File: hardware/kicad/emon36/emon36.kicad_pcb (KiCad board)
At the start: 4 copper layers, 80.6 x 104.1 mm, 236 parts, among them J1 MJ-3523-SMT, J10 MJ-3523-SMT, J11 MJ-3523-SMT, J12 MJ-3523-SMT, J13 MJ-3523-SMT, J14 MJ-3523-SMT, J15 MJ-3523-SMT, J16 MJ-3523-SMT, J17 MJ-3523-SMT, J18 MJ-3523-SMT, J19 MJ-3523-SMT, J2 MJ-3523-SMT, J20 MJ-3523-SMT, J21 MJ-3523-SMT, J22 MJ-3523-SMT, J23 MJ-3523-SMT, J24 MJ-3523-SMT, J25 MJ-3523-SMT, J26 MJ-3523-SMT, J27 MJ-3523-SMT, J28 MJ-3523-SMT, J29 MJ-3523-SMT, J3 MJ-3523-SMT, J30 MJ-3523-SMT, J31 MJ-3523-SMT, J32 MJ-3523-SMT, J33 MJ-3523-SMT, J34 MJ-3523-SMT, J35 MJ-3523-SMT, J36 MJ-3523-SMT, J4 MJ-3523-SMT, J5 MJ-3523-SMT, J6 MJ-3523-SMT, J7 MJ-3523-SMT, J8 MJ-3523-SMT, J9 MJ-3523-SMT, U1 ESP32-C3-WROOM-02-N4

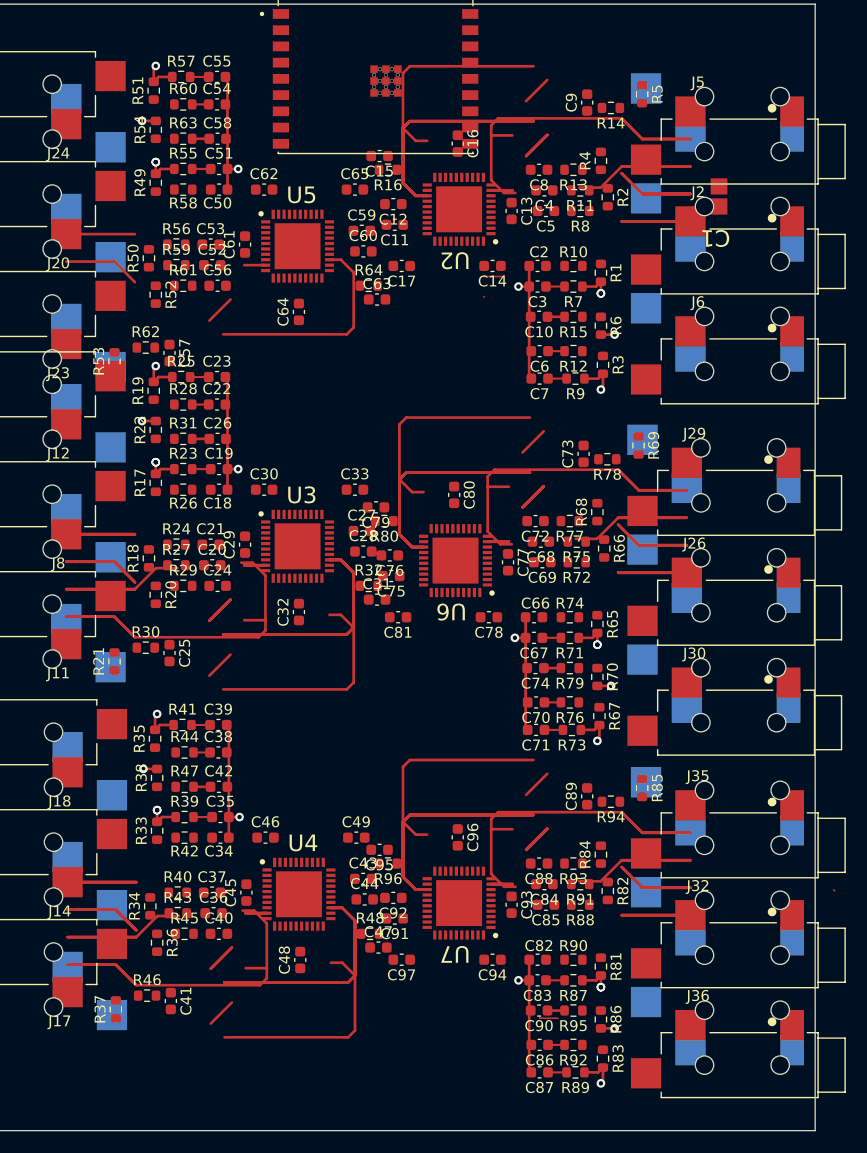
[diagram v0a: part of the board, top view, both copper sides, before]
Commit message: Add preliminary USB interface
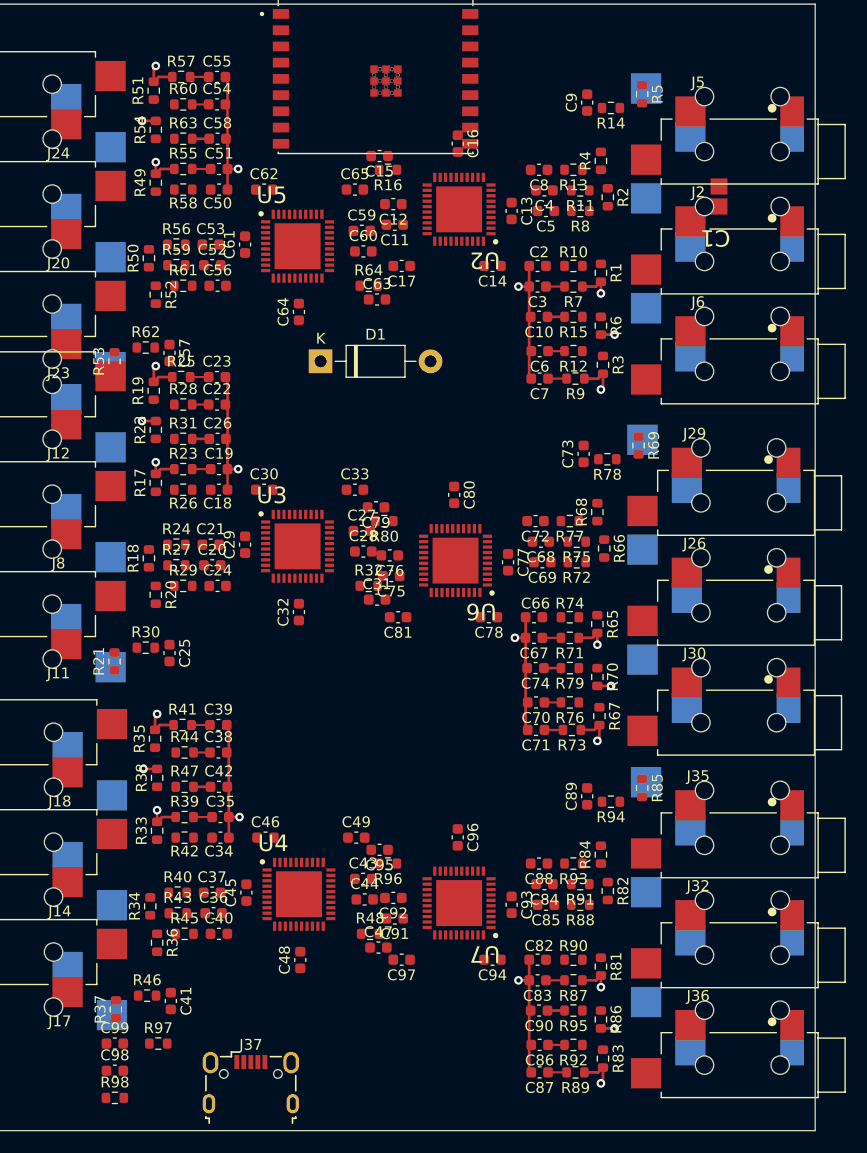
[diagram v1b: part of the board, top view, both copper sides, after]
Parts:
- added C98: 22pF, Capacitor_SMD:C_0603_1608Metric, F.Cu at (40.6, 140.1)
- added C99: 22pF, Capacitor_SMD:C_0603_1608Metric, F.Cu at (40.6, 137.6)
- added D1: 1N5819, Diode_THT:D_DO-41_SOD81_P10.16mm_Horizontal, F.Cu at (59.6, 74.5)
- added J37: USB_B_Micro, Connector_USB:USB_Micro-B_Wuerth_629105150521, F.Cu at (53.2, 141.2)
- added R97: 0, Resistor_SMD:R_0603_1608Metric, F.Cu at (44.6, 137.6)
- added R98: 0, Resistor_SMD:R_0603_1608Metric, F.Cu at (40.6, 142.6)
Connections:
- U1 pad 13: unconnected-(U1-Pad13) -> Net-(U1-Pad13)
- U1 pad 14: unconnected-(U1-Pad14) -> Net-(U1-Pad14)
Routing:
- net GND: track 304.4 -> 115.0 mm, vias 30 -> 24
- net /CH3/ID_P: track 113.0 -> 0.00 mm
- net /CH5/ID_P: track 113.0 -> 0.00 mm
- net /CH2/ID_P: track 110.2 -> 0.00 mm
- net /CH0/ID_P: track 110.2 -> 0.00 mm
- net /CH1/ID_P: track 92.8 -> 0.00 mm
- net Net-(J32-Pad2): track 36.5 -> 0.00 mm
- net Net-(J2-Pad2): track 36.5 -> 0.00 mm
- net Net-(J8-Pad2): track 36.5 -> 0.00 mm
- net Net-(J14-Pad2): track 36.5 -> 0.00 mm
- net Net-(J26-Pad2): track 36.5 -> 0.00 mm
- net /CH4/ID_P: track 30.0 -> 0.00 mm
- net unconnected-(U1-Pad15): track 20.1 -> 0.00 mm
- net Net-(J20-Pad2): track 6.35 -> 0.00 mm
- net /CH3/IB_P: track 5.94 -> 0.00 mm
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
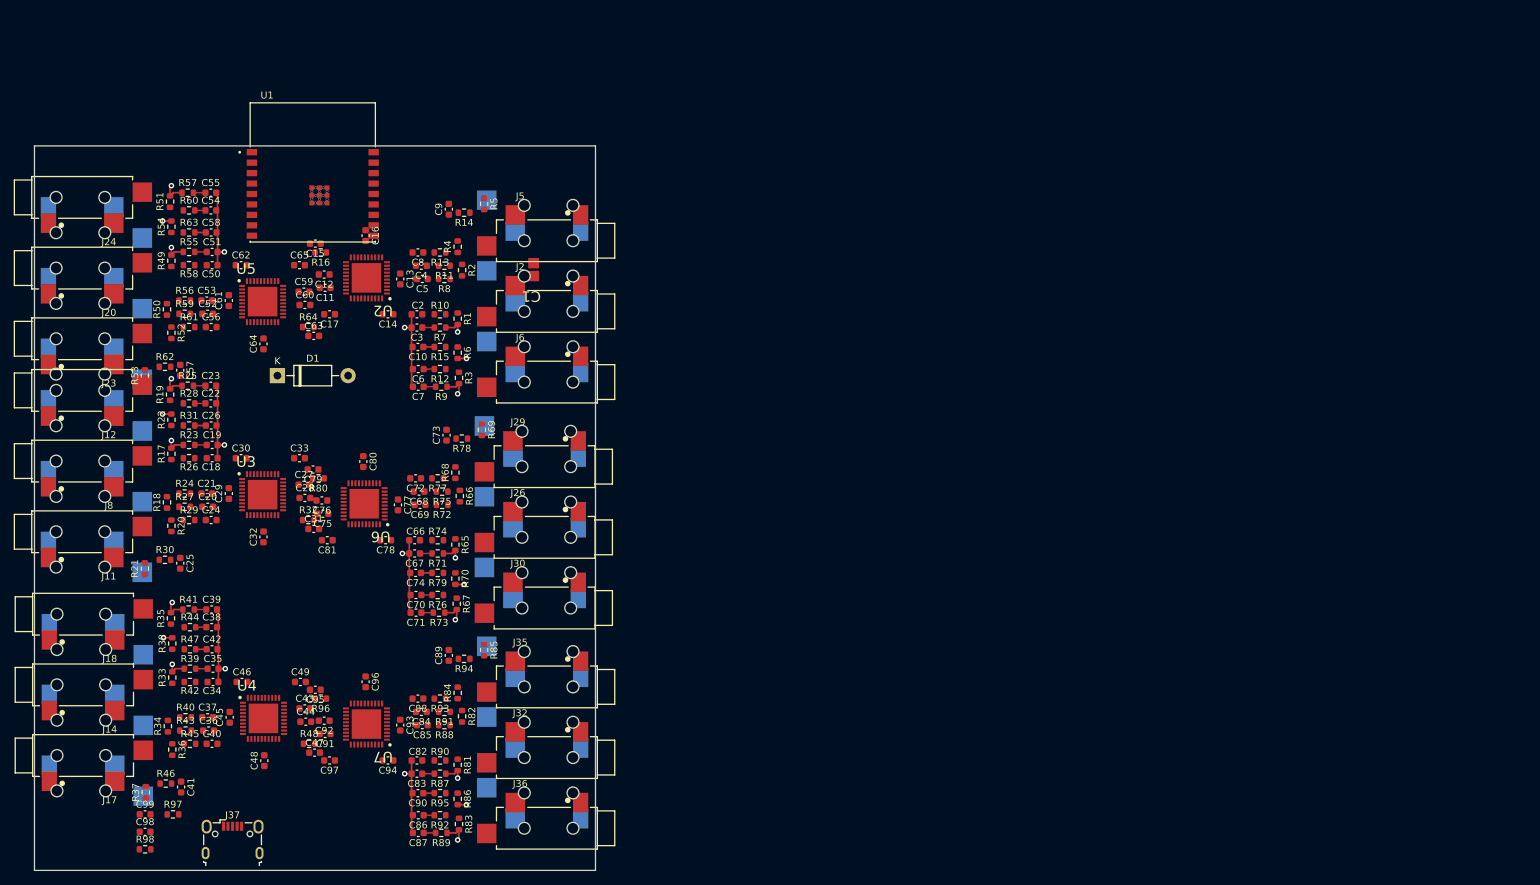
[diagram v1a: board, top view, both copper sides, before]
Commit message: Reverted to stacked 3.5mm connectors. Now has 42 channels. Added OLED, switches, power system. Cleaned up channel page.
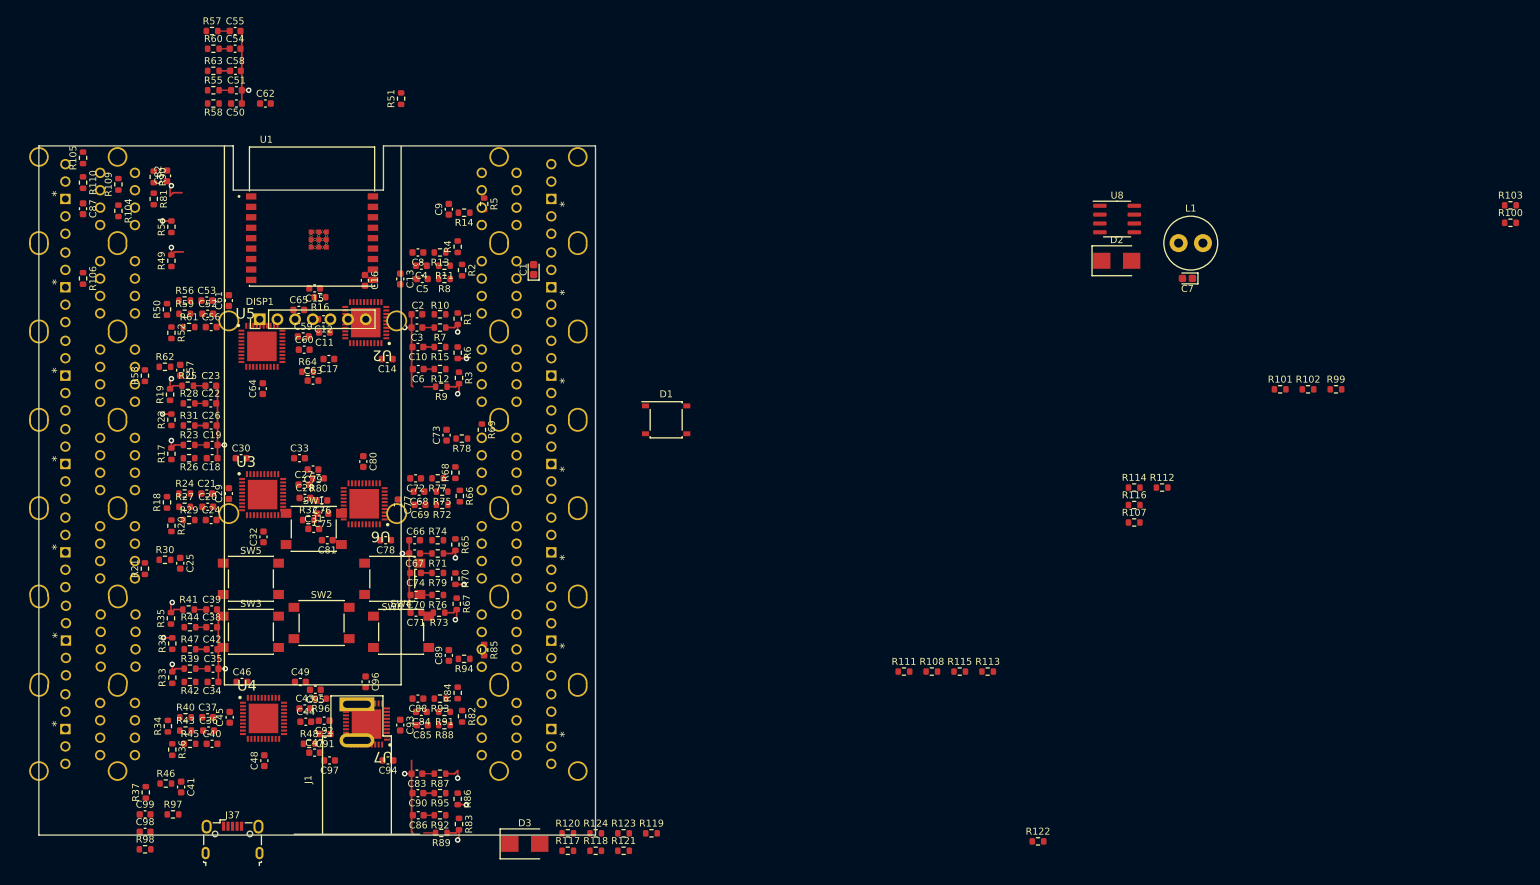
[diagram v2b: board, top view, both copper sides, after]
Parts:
- removed J16, J17, J18, J19, J20, J21, J22, J23, J24, J25, J26, J27, J28, J29, J30, J31, J32, J33, J34, J35, J36: MJ-3523-SMT, emon36:CUI_MJ-3523-SMT
- added D2: B240, Diode_SMD:D_SMB, F.Cu at (180.3, 58.0)
- added D3: B240, Diode_SMD:D_SMB, F.Cu at (95.2, 141.8)
- added DISP1: SSD1331_RGB_OLED_94x64, emon36:SSD1331_RGB_OLED_96x64, F.Cu at (64.7, 66.4)
- added L1: 82uH, Inductor_THT:L_Radial_D7.5mm_P3.50mm_Fastron_07P, F.Cu at (189.1, 55.5)
- added R100: 1k, Resistor_SMD:R_0603_1608Metric, F.Cu at (236.8, 52.6)
- added R101: 22, Resistor_SMD:R_0603_1608Metric, F.Cu at (203.7, 76.5)
- added R102: 22, Resistor_SMD:R_0603_1608Metric, F.Cu at (207.8, 76.5)
- added R103: 22, Resistor_SMD:R_0603_1608Metric, F.Cu at (236.8, 50.0)
- added R104: RB, Resistor_SMD:R_0603_1608Metric, F.Cu at (36.7, 50.8)
- added R105: RB, Resistor_SMD:R_0603_1608Metric, F.Cu at (31.7, 43.2)
- added R106: RB, Resistor_SMD:R_0603_1608Metric, F.Cu at (31.7, 60.6)
- added R107: RB, Resistor_SMD:R_0603_1608Metric, F.Cu at (182.8, 95.6)
- added R108: RB, Resistor_SMD:R_0603_1608Metric, F.Cu at (153.7, 117.1)
- added R109: 1k, Resistor_SMD:R_0603_1608Metric, F.Cu at (36.7, 47.0)
- added R110: 1k, Resistor_SMD:R_0603_1608Metric, F.Cu at (31.7, 46.8)
- added R111: 1k, Resistor_SMD:R_0603_1608Metric, F.Cu at (149.7, 117.1)
- added R112: 1k, Resistor_SMD:R_0603_1608Metric, F.Cu at (186.8, 90.6)
- added R113: 1k, Resistor_SMD:R_0603_1608Metric, F.Cu at (161.7, 117.1)
- added R114: 22, Resistor_SMD:R_0603_1608Metric, F.Cu at (182.8, 90.6)
- added R115: 22, Resistor_SMD:R_0603_1608Metric, F.Cu at (157.7, 117.1)
- added R116: 22, Resistor_SMD:R_0603_1608Metric, F.Cu at (182.8, 93.1)
- added R117: 75, Resistor_SMD:R_0603_1608Metric, F.Cu at (101.3, 142.8)
- added R118: 75, Resistor_SMD:R_0603_1608Metric, F.Cu at (105.4, 142.8)
- added R119: 2.2k, Resistor_SMD:R_0603_1608Metric, F.Cu at (113.4, 140.3)
- added R120: 2.2k, Resistor_SMD:R_0603_1608Metric, F.Cu at (101.3, 140.3)
- added R121: 2.2k, Resistor_SMD:R_0603_1608Metric, F.Cu at (109.4, 142.8)
- added R122: 2.2k, Resistor_SMD:R_0603_1608Metric, F.Cu at (168.9, 141.5)
- added R123: 2.2k, Resistor_SMD:R_0603_1608Metric, F.Cu at (109.4, 140.3)
- added R124: 2.2k, Resistor_SMD:R_0603_1608Metric, F.Cu at (105.4, 140.3)
- added R99: 1k, Resistor_SMD:R_0603_1608Metric, F.Cu at (211.8, 76.5)
- added SW1: SW_MEC_5E, Button_Switch_SMD:SW_Push_1P1T_NO_6x6mm_H13mm, F.Cu at (64.8, 96.6)
- added SW2: SW_MEC_5E, Button_Switch_SMD:SW_Push_1P1T_NO_6x6mm_H13mm, F.Cu at (66.0, 110.1)
- added SW3: SW_MEC_5E, Button_Switch_SMD:SW_Push_1P1T_NO_6x6mm_H13mm, F.Cu at (55.8, 111.4)
- added SW4: SW_MEC_5E, Button_Switch_SMD:SW_Push_1P1T_NO_6x6mm_H13mm, F.Cu at (77.4, 111.4)
- added SW5: SW_MEC_5E, Button_Switch_SMD:SW_Push_1P1T_NO_6x6mm_H13mm, F.Cu at (55.8, 103.7)
- added SW6: SW_MEC_5E, Button_Switch_SMD:SW_Push_1P1T_NO_6x6mm_H13mm, F.Cu at (76.1, 103.7)
- added U8: TPS54233, Package_SO:SOIC-8_3.9x4.9mm_P1.27mm, F.Cu at (180.3, 52.0)
- C1: value VJ0805Y472KXBBC31 -> 100uF/25V; footprint emon36:CAPC2013X145X48ML20T23 -> Capacitor_Tantalum_SMD:CP_EIA-1608-08_AVX-J
- C11, C43, C48, C59: value 4.7uF -> 22nF
- C12, C44, C60: value 0.22uF -> 22nF
- C19, C26, C39, C41, C52, C54, C67, C84: value 22nF -> 4.7uF
- C20, C42, C55, C68, C85: value 22nF -> 0.22uF
- C27: value 4.7uF -> 0.1uF
- C28, C76: value 0.22uF -> 4.7uF
- C3, C6: value 22nF -> 10uF/25V
- C32, C80: value 4.7uF -> 0.22uF
- C33, C49: value 0.1uF -> 22nF
- C4: value 22nF -> 2.2nF
- C40, C53: value 22nF -> 0.1uF
- C5: value 22nF -> 10nF
- C7: value 22nF -> 220uF/25V; footprint Capacitor_SMD:C_0603_1608Metric -> Capacitor_Tantalum_SMD:CP_EIA-1608-08_AVX-J
- C92: value 0.22uF -> 0.1uF
- C97: value 0.1uF -> 0.22uF
- D1: value 1N5819 -> ABS6; footprint Diode_THT:D_DO-41_SOD81_P10.16mm_Horizontal -> Diode_SMD:Diode_Bridge_Diotec_ABS
- J1: value MJ-3523-SMT -> Barrel_Jack; footprint emon36:CUI_MJ-3523-SMT -> Connector_BarrelJack:BarrelJack_SwitchcraftConxall_RAPC10U_Horizontal; moved to F.Cu
- J10, J13, J15, J3, J4, J7, J9: value MJ-3523-SMT -> STX-4335-5BGP-S1; footprint emon36:CUI_MJ-3523-SMT -> Connector_Audio:STX-4335-5BGP-S1_KYC
- J11, J12, J14, J2, J5, J6, J8: value MJ-3523-SMT -> STX-4335-5BGP-S1; footprint emon36:CUI_MJ-3523-SMT -> Connector_Audio:STX-4335-5BGP-S1_KYC; moved to B.Cu
- R15, R31, R47, R63, R79: value 1k -> 22
- R18, R19, R34, R35, R50, R51, R66, R67, R82, R83: value RB -> 22
- R2: value RB -> 0
- R23, R24, R39, R40, R55, R56, R7, R71, R72, R8, R87, R88, R89: value 1k -> RB
- R3: value RB -> 47k
- moved C7 111.7 mm to (190.4, 60.6)
- moved C87 101.8 mm to (31.7, 50.5), turned to -90 degrees
- moved J13 100.7 mm to (99.0, 49.1), turned to 90 degrees
- moved R90 93.4 mm to (41.8, 45.9), turned to 90 degrees
- moved R81 92.3 mm to (41.8, 49.1)
- moved C82 91.4 mm to (43.7, 45.8), turned to -90 degrees
- moved J5 89.9 mm to (29.2, 112.6), turned to -90 degrees
- moved J4 85.3 mm to (29.1, 99.9), turned to -90 degrees
- moved J6 85.3 mm to (29.1, 125.3), turned to -90 degrees
- moved J7 75.3 mm to (99.0, 125.3), turned to 90 degrees
- moved J8 72.2 mm to (99.0, 112.6), turned to 90 degrees
- moved J3 71.2 mm to (29.1, 87.2), turned to -90 degrees
- moved J11 71.1 mm to (99.0, 74.5), turned to 90 degrees
- moved J14 69.9 mm to (29.1, 49.1), turned to -90 degrees
- moved J9 69.8 mm to (99.0, 99.9), turned to 90 degrees
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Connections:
- net /CS0 renamed /SPI_CS0
- net Net-(C98-Pad1) renamed /USB_D-
- net Net-(C99-Pad1) renamed /USB_D+
- C1 pad 1: GND -> Net-(C1-Pad1)
- C1 pad 2: 3V3 -> GND
- C10 pad 1: /CH1/IF_P -> /CH1/ID_P
- C11 pad 1: Net-(C11-Pad1) -> /CH1/IE_P
- C12 pad 1: Net-(C11-Pad1) -> /CH1/IF_P
- C19 pad 1: /CH2/IA_N -> Net-(C19-Pad1)
- C20 pad 1: /CH2/IB_P -> Net-(C19-Pad1)
- C21 pad 1: /CH2/IB_N -> /CH2/IB_P
- C23 pad 1: /CH2/IC_N -> /CH2/ID_P
- C24 pad 1: /CH2/ID_P -> /CH2/IE_P
- C25 pad 1: /CH2/IE_P -> /CH2/IF_P
- C26 pad 1: /CH2/IF_P -> Net-(C26-Pad1)
- C27 pad 1: Net-(C27-Pad1) -> Net-(C26-Pad1)
- C28 pad 1: Net-(C27-Pad1) -> Net-(C28-Pad1)
- C3 pad 1: /CH1/IA_N -> Net-(C1-Pad1)
- C32 pad 1: Net-(C32-Pad1) -> Net-(C28-Pad1)
- C33 pad 1: Net-(C32-Pad1) -> /CH3/IB_P
- C35 pad 1: /CH3/IA_N -> /CH3/IC_P
- C36 pad 1: /CH3/IB_P -> /CH3/ID_P
- C37 pad 1: /CH3/IB_N -> /CH3/IE_P
- C38 pad 1: /CH3/IC_P -> /CH3/IF_P
- C39 pad 1: /CH3/IC_N -> Net-(C39-Pad1)
- C4 pad 1: /CH1/IB_P -> Net-(C4-Pad1)
- C40 pad 1: /CH3/ID_P -> Net-(C39-Pad1)
- C41 pad 1: /CH3/IE_P -> Net-(C41-Pad1)
- C42 pad 1: /CH3/IF_P -> Net-(C41-Pad1)
- C43 pad 1: Net-(C43-Pad1) -> /CH4/IB_P
- C44 pad 1: Net-(C43-Pad1) -> /CH4/IC_P
- C48 pad 1: Net-(C48-Pad1) -> /CH4/ID_P
- C49 pad 1: Net-(C48-Pad1) -> /CH4/IE_P
- C5 pad 1: /CH1/IB_N -> Net-(C5-Pad1)
- C51 pad 1: /CH4/IA_N -> /CH4/IF_P
- C52 pad 1: /CH4/IB_P -> Net-(C52-Pad1)
- C53 pad 1: /CH4/IB_N -> Net-(C52-Pad1)
- C54 pad 1: /CH4/IC_P -> Net-(C54-Pad1)
- C55 pad 1: /CH4/IC_N -> Net-(C54-Pad1)
- C56 pad 1: /CH4/ID_P -> /CH5/IB_P
- C57 pad 1: /CH4/IE_P -> /CH5/IC_P
- C58 pad 1: /CH4/IF_P -> /CH5/ID_P
- C59 pad 1: Net-(C59-Pad1) -> /CH5/IE_P
- C6 pad 1: /CH1/IC_P -> Net-(C6-Pad1)
- C6 pad 2: GND -> Net-(C6-Pad2)
- C60 pad 1: Net-(C59-Pad1) -> /CH5/IF_P
- C67 pad 1: /CH5/IA_N -> Net-(C67-Pad1)
- C68 pad 1: /CH5/IB_P -> Net-(C67-Pad1)
- C69 pad 1: /CH5/IB_N -> /CH7/IA_P
- C7 pad 1: /CH1/IC_N -> 3V3
- C70 pad 1: /CH5/IC_P -> /CH7/IB_P
- C71 pad 1: /CH5/IC_N -> /CH7/IC_P
- C72 pad 1: /CH5/ID_P -> /CH7/ID_P
- C73 pad 1: /CH5/IE_P -> /CH7/IE_P
- C74 pad 1: /CH5/IF_P -> /CH7/IF_P
- C76 pad 1: Net-(C75-Pad1) -> Net-(C76-Pad1)
- C8 pad 1: /CH1/ID_P -> /CH1/IB_P
- C80 pad 1: Net-(C80-Pad1) -> Net-(C75-Pad1)
- C81 pad 1: Net-(C80-Pad1) -> Net-(C76-Pad1)
- C83 pad 1: /CH0/IA_N -> Net-(C83-Pad1)
- C84 pad 1: /CH0/IB_P -> Net-(C84-Pad1)
- C85 pad 1: /CH0/IB_N -> Net-(C84-Pad1)
- C86 pad 1: /CH0/IC_P -> /CH0/IB_P
- C87 pad 1: /CH0/IC_N -> /CH0/IC_P
- C9 pad 1: /CH1/IE_P -> /CH1/IC_P
- D1 pad 1: +5V -> Net-(C1-Pad1)
- D1 pad 2: Net-(D1-Pad2) -> GND
- J1 pad 1: GND -> Net-(D1-Pad4)
- J1 pad 2: Net-(J1-Pad2) -> Net-(D1-Pad3)
- J10 pad 2: Net-(J10-Pad2) -> unconnected-(J10-Pad2)
- J11 pad 2: Net-(J11-Pad2) -> unconnected-(J11-Pad2)
- J12 pad 2: Net-(J12-Pad2) -> unconnected-(J12-Pad2)
- J13 pad 2: Net-(J13-Pad2) -> unconnected-(J13-Pad2)
- J14 pad 2: Net-(J14-Pad2) -> unconnected-(J14-Pad2)
- J15 pad 2: Net-(J15-Pad2) -> unconnected-(J15-Pad2)
- J2 pad 2: Net-(J2-Pad2) -> unconnected-(J2-Pad2)
- J3 pad 2: Net-(J3-Pad2) -> unconnected-(J3-Pad2)
- J4 pad 2: Net-(J4-Pad2) -> unconnected-(J4-Pad2)
- J5 pad 2: Net-(J5-Pad2) -> unconnected-(J5-Pad2)
- J6 pad 2: Net-(J6-Pad2) -> unconnected-(J6-Pad2)
- J7 pad 2: Net-(J7-Pad2) -> unconnected-(J7-Pad2)
- J8 pad 2: Net-(J8-Pad2) -> unconnected-(J8-Pad2)
- J9 pad 2: Net-(J9-Pad2) -> unconnected-(J9-Pad2)
- R1 pad 1: Net-(J1-Pad2) -> Net-(J2-Pad35)
- R10 pad 1: Net-(J1-Pad2) -> Net-(J2-Pad35)
- R11 pad 1: Net-(J2-Pad2) -> Net-(J2-Pad5)
- R11 pad 2: /CH1/IB_P -> /CH1/IC_P
- R12 pad 1: Net-(J3-Pad2) -> Net-(J3-Pad35)
- R12 pad 2: /CH1/IC_P -> /CH1/ID_P
- R13 pad 1: Net-(J4-Pad2) -> Net-(J3-Pad25)
- R13 pad 2: /CH1/ID_P -> /CH1/IE_P
- R14 pad 1: Net-(J5-Pad2) -> Net-(J3-Pad5)
- R14 pad 2: /CH1/IE_P -> /CH1/IF_P
- R15 pad 1: Net-(J6-Pad2) -> Net-(R15-Pad1)
- R15 pad 2: /CH1/IF_P -> /MISO
- R17 pad 1: Net-(J7-Pad2) -> Net-(J4-Pad35)
- R18 pad 1: Net-(J8-Pad2) -> Net-(R18-Pad1)
- R18 pad 2: GND -> /CH1/IRQ
- R19 pad 1: Net-(J9-Pad2) -> Net-(R19-Pad1)
- R19 pad 2: GND -> /CH1/IRQ
- R2 pad 1: Net-(J2-Pad2) -> Net-(R2-Pad1)
- R20 pad 1: Net-(J10-Pad2) -> Net-(J4-Pad25)
- R21 pad 1: Net-(J11-Pad2) -> Net-(J4-Pad5)
- R22 pad 1: Net-(J12-Pad2) -> Net-(J5-Pad35)
- R23 pad 1: GND -> Net-(J5-Pad25)
- R23 pad 2: /CH2/IA_N -> GND
- R24 pad 1: GND -> Net-(J5-Pad5)
- R24 pad 2: /CH2/IB_N -> GND
- R25 pad 1: GND -> Net-(J4-Pad25)
- R25 pad 2: /CH2/IC_N -> /CH2/IB_P
- R26 pad 1: Net-(J7-Pad2) -> Net-(J4-Pad35)
- R27 pad 1: Net-(J8-Pad2) -> Net-(J4-Pad5)
- R27 pad 2: /CH2/IB_P -> /CH2/IC_P
- R28 pad 1: Net-(J9-Pad2) -> Net-(J5-Pad35)
- R28 pad 2: /CH2/IC_P -> /CH2/ID_P
- R29 pad 1: Net-(J10-Pad2) -> Net-(J5-Pad25)
- R29 pad 2: /CH2/ID_P -> /CH2/IE_P
- R3 pad 1: Net-(J3-Pad2) -> Net-(R3-Pad1)
- R3 pad 2: GND -> Net-(C4-Pad1)
- R30 pad 1: Net-(J11-Pad2) -> Net-(J5-Pad5)
- R30 pad 2: /CH2/IE_P -> /CH2/IF_P
- R31 pad 1: Net-(J12-Pad2) -> Net-(R31-Pad1)
- R31 pad 2: /CH2/IF_P -> /MISO
- R33 pad 1: Net-(J13-Pad2) -> Net-(J6-Pad35)
- R34 pad 1: Net-(J14-Pad2) -> Net-(R34-Pad1)
- R34 pad 2: GND -> /CH2/IRQ
- R35 pad 1: Net-(J15-Pad2) -> Net-(R35-Pad1)
- R35 pad 2: GND -> /CH2/IRQ
- R36 pad 1: Net-(J16-Pad2) -> Net-(J6-Pad25)
- R37 pad 1: Net-(J17-Pad2) -> Net-(J6-Pad5)
- R38 pad 1: Net-(J18-Pad2) -> Net-(J7-Pad35)
- R39 pad 1: GND -> Net-(J7-Pad25)
- R39 pad 2: /CH3/IA_N -> GND
- R4 pad 1: Net-(J4-Pad2) -> Net-(J2-Pad25)
- R40 pad 1: GND -> Net-(J7-Pad5)
- R40 pad 2: /CH3/IB_N -> GND
- R41 pad 1: GND -> Net-(J6-Pad25)
- R41 pad 2: /CH3/IC_N -> /CH3/IB_P
- R42 pad 1: Net-(J13-Pad2) -> Net-(J6-Pad35)
- R43 pad 1: Net-(J14-Pad2) -> Net-(J6-Pad5)
- R43 pad 2: /CH3/IB_P -> /CH3/IC_P
- R44 pad 1: Net-(J15-Pad2) -> Net-(J7-Pad35)
- R44 pad 2: /CH3/IC_P -> /CH3/ID_P
- R45 pad 1: Net-(J16-Pad2) -> Net-(J7-Pad25)
- R45 pad 2: /CH3/ID_P -> /CH3/IE_P
- R46 pad 1: Net-(J17-Pad2) -> Net-(J7-Pad5)
- R46 pad 2: /CH3/IE_P -> /CH3/IF_P
- R47 pad 1: Net-(J18-Pad2) -> Net-(R47-Pad1)
- R47 pad 2: /CH3/IF_P -> /MISO
- R49 pad 1: Net-(J19-Pad2) -> Net-(J8-Pad35)
- R5 pad 1: Net-(J5-Pad2) -> Net-(J2-Pad5)
- R50 pad 1: Net-(J20-Pad2) -> Net-(R50-Pad1)
- R50 pad 2: GND -> /CH3/IRQ
- R51 pad 1: Net-(J21-Pad2) -> Net-(R51-Pad1)
- R51 pad 2: GND -> /CH3/IRQ
- R52 pad 1: Net-(J22-Pad2) -> Net-(J8-Pad25)
- R53 pad 1: Net-(J23-Pad2) -> Net-(J8-Pad5)
- R54 pad 1: Net-(J24-Pad2) -> Net-(J9-Pad35)
- R55 pad 1: GND -> Net-(J9-Pad25)
- R55 pad 2: /CH4/IA_N -> GND
- R56 pad 1: GND -> Net-(J9-Pad5)
- R56 pad 2: /CH4/IB_N -> GND
- R57 pad 1: GND -> Net-(J8-Pad25)
- R57 pad 2: /CH4/IC_N -> /CH4/IB_P
- R58 pad 1: Net-(J19-Pad2) -> Net-(J8-Pad35)
- R59 pad 1: Net-(J20-Pad2) -> Net-(J8-Pad5)
- R59 pad 2: /CH4/IB_P -> /CH4/IC_P
- R6 pad 1: Net-(J6-Pad2) -> Net-(J3-Pad35)
- R60 pad 1: Net-(J21-Pad2) -> Net-(J9-Pad35)
- R60 pad 2: /CH4/IC_P -> /CH4/ID_P
- R61 pad 1: Net-(J22-Pad2) -> Net-(J9-Pad25)
- R61 pad 2: /CH4/ID_P -> /CH4/IE_P
- R62 pad 1: Net-(J23-Pad2) -> Net-(J9-Pad5)
- R62 pad 2: /CH4/IE_P -> /CH4/IF_P
- R63 pad 1: Net-(J24-Pad2) -> Net-(R63-Pad1)
- R63 pad 2: /CH4/IF_P -> /MISO
- R65 pad 1: Net-(J25-Pad2) -> Net-(J10-Pad35)
- R66 pad 1: Net-(J26-Pad2) -> Net-(R66-Pad1)
- R66 pad 2: GND -> /CH4/IRQ
- R67 pad 1: Net-(J27-Pad2) -> Net-(R67-Pad1)
- R67 pad 2: GND -> /CH4/IRQ
- R68 pad 1: Net-(J28-Pad2) -> Net-(J10-Pad25)
- R69 pad 1: Net-(J29-Pad2) -> Net-(J10-Pad5)
- R7 pad 1: GND -> Net-(J3-Pad25)
- R7 pad 2: /CH1/IA_N -> GND
- R70 pad 1: Net-(J30-Pad2) -> Net-(J11-Pad35)
- R71 pad 1: GND -> Net-(J11-Pad25)
- R71 pad 2: /CH5/IA_N -> GND
- R72 pad 1: GND -> Net-(J11-Pad5)
- R72 pad 2: /CH5/IB_N -> GND
- R73 pad 1: GND -> Net-(J10-Pad25)
- R73 pad 2: /CH5/IC_N -> /CH5/IB_P
- R74 pad 1: Net-(J25-Pad2) -> Net-(J10-Pad35)
- R75 pad 1: Net-(J26-Pad2) -> Net-(J10-Pad5)
- R75 pad 2: /CH5/IB_P -> /CH5/IC_P
- R76 pad 1: Net-(J27-Pad2) -> Net-(J11-Pad35)
- R76 pad 2: /CH5/IC_P -> /CH5/ID_P
- R77 pad 1: Net-(J28-Pad2) -> Net-(J11-Pad25)
- R77 pad 2: /CH5/ID_P -> /CH5/IE_P
- R78 pad 1: Net-(J29-Pad2) -> Net-(J11-Pad5)
- R78 pad 2: /CH5/IE_P -> /CH5/IF_P
- R79 pad 1: Net-(J30-Pad2) -> Net-(R79-Pad1)
- R79 pad 2: /CH5/IF_P -> /MISO
- R8 pad 1: GND -> Net-(J3-Pad5)
- R8 pad 2: /CH1/IB_N -> GND
- R81 pad 1: Net-(J31-Pad2) -> Net-(J14-Pad35)
- R82 pad 1: Net-(J32-Pad2) -> Net-(R82-Pad1)
- R82 pad 2: GND -> /CH5/IRQ
- R83 pad 1: Net-(J33-Pad2) -> Net-(R83-Pad1)
- R83 pad 2: GND -> /CH5/IRQ
- R84 pad 1: Net-(J34-Pad2) -> Net-(J12-Pad35)
- R85 pad 1: Net-(J35-Pad2) -> Net-(J12-Pad25)
- R86 pad 1: Net-(J36-Pad2) -> Net-(J12-Pad5)
- R87 pad 1: GND -> Net-(J13-Pad35)
- R87 pad 2: /CH0/IA_N -> GND
- R88 pad 1: GND -> Net-(J13-Pad25)
- R88 pad 2: /CH0/IB_N -> GND
- R89 pad 1: GND -> Net-(J13-Pad5)
- R89 pad 2: /CH0/IC_N -> GND
- R9 pad 1: GND -> Net-(J2-Pad25)
- R9 pad 2: /CH1/IC_N -> /CH1/IB_P
- R90 pad 1: Net-(J31-Pad2) -> Net-(J14-Pad35)
- R91 pad 1: Net-(J32-Pad2) -> Net-(J12-Pad35)
- R91 pad 2: /CH0/IB_P -> /CH7/IA_P
- R92 pad 1: Net-(J33-Pad2) -> Net-(J12-Pad25)
- R92 pad 2: /CH0/IC_P -> /CH7/IB_P
- R93 pad 1: Net-(J34-Pad2) -> Net-(J12-Pad5)
- R93 pad 2: /CH0/ID_P -> /CH7/IC_P
- R94 pad 1: Net-(J35-Pad2) -> Net-(J13-Pad35)
- R94 pad 2: /CH0/IE_P -> /CH7/ID_P
- R95 pad 1: Net-(J36-Pad2) -> Net-(J13-Pad25)
- R95 pad 2: /CH0/IF_P -> /CH7/IE_P
- U1 pad 11: unconnected-(U1-Pad11) -> /SPI_CS7
- U1 pad 12: unconnected-(U1-Pad12) -> /SPI_CS6
- U1 pad 15: unconnected-(U1-Pad15) -> /SPI_CS3
- U1 pad 16: /MOSI -> /SPI_MISO
- U1 pad 17: unconnected-(U1-Pad17) -> /OLED_C/~{D}
- U1 pad 18: unconnected-(U1-Pad18) -> /OLED_RES
- U1 pad 3: unconnected-(U1-Pad3) -> /SPI_CS5
- U1 pad 4: unconnected-(U1-Pad4) -> /SPI_CS4
- U1 pad 6: /MISO -> /SPI_MOSI
- U1 pad 7: unconnected-(U1-Pad7) -> /SPI_CS2
- U1 pad 8: unconnected-(U1-Pad8) -> /SPI_CS1
- U2 pad 12: /CH1/IB_N -> Net-(C15-Pad1)
- U2 pad 14: /CH1/IC_N -> Net-(C15-Pad1)
- U2 pad 16: unconnected-(U2-Pad16) -> Net-(C15-Pad1)
- U2 pad 24: Net-(C11-Pad1) -> Net-(C13-Pad1)
- U2 pad 29: unconnected-(U2-Pad29) -> Net-(R19-Pad1)
- U2 pad 32: unconnected-(U2-Pad32) -> Net-(R18-Pad1)
- U2 pad 35: /SCLK -> unconnected-(U2-Pad35)
- U2 pad 36: unconnected-(U2-Pad36) -> /SPI_SCLK
- U2 pad 37: /MISO -> Net-(R15-Pad1)
- U2 pad 38: /MOSI -> /SPI_MOSI
- U2 pad 39: /CS1 -> /SPI_CS1
- U2 pad 4: unconnected-(U2-Pad4) -> /CH1/RESET
- U2 pad 5: Net-(C13-Pad1) -> Net-(C19-Pad1)
- U2 pad 8: /CH1/IA_N -> Net-(C15-Pad1)
- U3 pad 12: /CH2/IB_N -> Net-(C31-Pad1)
- U3 pad 14: /CH2/IC_N -> Net-(C31-Pad1)
- U3 pad 16: unconnected-(U3-Pad16) -> Net-(C31-Pad1)
- U3 pad 17: Net-(C32-Pad1) -> Net-(C26-Pad1)
- U3 pad 24: Net-(C27-Pad1) -> Net-(C29-Pad1)
- U3 pad 29: unconnected-(U3-Pad29) -> Net-(R35-Pad1)
- U3 pad 32: unconnected-(U3-Pad32) -> Net-(R34-Pad1)
- U3 pad 35: /SCLK -> unconnected-(U3-Pad35)
- U3 pad 36: unconnected-(U3-Pad36) -> /SPI_SCLK
- U3 pad 37: /MISO -> Net-(R31-Pad1)
- U3 pad 38: /MOSI -> /SPI_MOSI
- U3 pad 39: /CS2 -> /SPI_CS2
- U3 pad 4: unconnected-(U3-Pad4) -> /CH2/RESET
- U3 pad 5: Net-(C29-Pad1) -> Net-(C28-Pad1)
- U3 pad 8: /CH2/IA_N -> Net-(C31-Pad1)
- U4 pad 12: /CH3/IB_N -> Net-(C47-Pad1)
- U4 pad 14: /CH3/IC_N -> Net-(C47-Pad1)
- U4 pad 16: unconnected-(U4-Pad16) -> Net-(C47-Pad1)
- U4 pad 17: Net-(C48-Pad1) -> Net-(C39-Pad1)
- U4 pad 24: Net-(C43-Pad1) -> Net-(C45-Pad1)
- U4 pad 29: unconnected-(U4-Pad29) -> Net-(R51-Pad1)
- U4 pad 32: unconnected-(U4-Pad32) -> Net-(R50-Pad1)
- U4 pad 35: /SCLK -> unconnected-(U4-Pad35)
- U4 pad 36: unconnected-(U4-Pad36) -> /SPI_SCLK
- U4 pad 37: /MISO -> Net-(R47-Pad1)
- U4 pad 38: /MOSI -> /SPI_MOSI
- U4 pad 39: /CS3 -> /SPI_CS3
- U4 pad 4: unconnected-(U4-Pad4) -> /CH3/RESET
- U4 pad 5: Net-(C45-Pad1) -> Net-(C41-Pad1)
- U4 pad 8: /CH3/IA_N -> Net-(C47-Pad1)
- U5 pad 12: /CH4/IB_N -> Net-(C63-Pad1)
- U5 pad 14: /CH4/IC_N -> Net-(C63-Pad1)
- U5 pad 16: unconnected-(U5-Pad16) -> Net-(C63-Pad1)
- U5 pad 17: Net-(C64-Pad1) -> Net-(C52-Pad1)
- U5 pad 24: Net-(C59-Pad1) -> Net-(C61-Pad1)
- U5 pad 29: unconnected-(U5-Pad29) -> Net-(R67-Pad1)
- U5 pad 32: unconnected-(U5-Pad32) -> Net-(R66-Pad1)
- U5 pad 35: /SCLK -> unconnected-(U5-Pad35)
- U5 pad 36: unconnected-(U5-Pad36) -> /SPI_SCLK
- U5 pad 37: /MISO -> Net-(R63-Pad1)
- U5 pad 38: /MOSI -> /SPI_MOSI
- U5 pad 39: /CS4 -> /SPI_CS4
- U5 pad 4: unconnected-(U5-Pad4) -> /CH4/RESET
- U5 pad 5: Net-(C61-Pad1) -> Net-(C54-Pad1)
- U5 pad 8: /CH4/IA_N -> Net-(C63-Pad1)
- U6 pad 12: /CH5/IB_N -> Net-(C79-Pad1)
- U6 pad 14: /CH5/IC_N -> Net-(C79-Pad1)
- U6 pad 16: unconnected-(U6-Pad16) -> Net-(C79-Pad1)
- U6 pad 17: Net-(C80-Pad1) -> Net-(C64-Pad1)
- U6 pad 24: Net-(C75-Pad1) -> Net-(C77-Pad1)
- U6 pad 29: unconnected-(U6-Pad29) -> Net-(R83-Pad1)
- U6 pad 32: unconnected-(U6-Pad32) -> Net-(R82-Pad1)
- U6 pad 35: /SCLK -> unconnected-(U6-Pad35)
- U6 pad 36: unconnected-(U6-Pad36) -> /SPI_SCLK
- U6 pad 37: /MISO -> Net-(R79-Pad1)
- U6 pad 38: /MOSI -> /SPI_MOSI
- U6 pad 39: /CS5 -> /SPI_CS5
- U6 pad 4: unconnected-(U6-Pad4) -> /CH5/RESET
- U6 pad 5: Net-(C77-Pad1) -> Net-(C67-Pad1)
- U6 pad 8: /CH5/IA_N -> Net-(C79-Pad1)
- U7 pad 12: /CH0/IB_N -> Net-(C95-Pad1)
- U7 pad 14: /CH0/IC_N -> Net-(C95-Pad1)
- U7 pad 16: unconnected-(U7-Pad16) -> Net-(C95-Pad1)
- U7 pad 17: Net-(C96-Pad1) -> Net-(C91-Pad1)
- U7 pad 24: Net-(C91-Pad1) -> Net-(C93-Pad1)
- U7 pad 29: unconnected-(U7-Pad29) -> Net-(R116-Pad1)
- U7 pad 32: unconnected-(U7-Pad32) -> Net-(R115-Pad1)
- U7 pad 35: /SCLK -> unconnected-(U7-Pad35)
- U7 pad 36: unconnected-(U7-Pad36) -> /SPI_SCLK
- U7 pad 37: /MISO -> Net-(R114-Pad1)
- U7 pad 38: /MOSI -> /SPI_MOSI
- U7 pad 4: unconnected-(U7-Pad4) -> /CH0/RESET
- U7 pad 5: Net-(C93-Pad1) -> Net-(C96-Pad1)
- U7 pad 8: /CH0/IA_N -> Net-(C95-Pad1)
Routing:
- net GND: track 115.0 -> 100.0 mm, vias 24 -> 18
- net /MISO: track 0.00 -> 4.72 mm
- net Net-(C4-Pad1): track 0.00 -> 3.44 mm, vias 0 -> 1
- net /CH4/IRQ: track 0.00 -> 3.44 mm, vias 0 -> 1
- net /CH2/IRQ: track 0.00 -> 3.44 mm, vias 0 -> 1
- net /CH1/IRQ: track 0.00 -> 3.44 mm, vias 0 -> 1
- net /CH5/IRQ: track 0.00 -> 3.44 mm, vias 0 -> 1
- net /CH1/ID_P: track 0.00 -> 3.10 mm
- net Net-(J13-Pad35): track 0.00 -> 2.98 mm, vias 0 -> 1
- net Net-(C83-Pad1): track 0.00 -> 1.72 mm
- net Net-(C54-Pad1): track 0.00 -> 1.72 mm
- net Net-(C39-Pad1): track 0.00 -> 1.72 mm
- net /CH7/IC_P: track 0.00 -> 1.72 mm
- net /CH5/IC_N: track 1.72 -> 0.00 mm
- net /CH4/IC_N: track 1.72 -> 0.00 mm
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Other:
- board size 80.6 x 104.1 mm -> 80 x 99.1 mm
